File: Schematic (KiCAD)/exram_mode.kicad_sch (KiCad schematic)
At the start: 94 parts

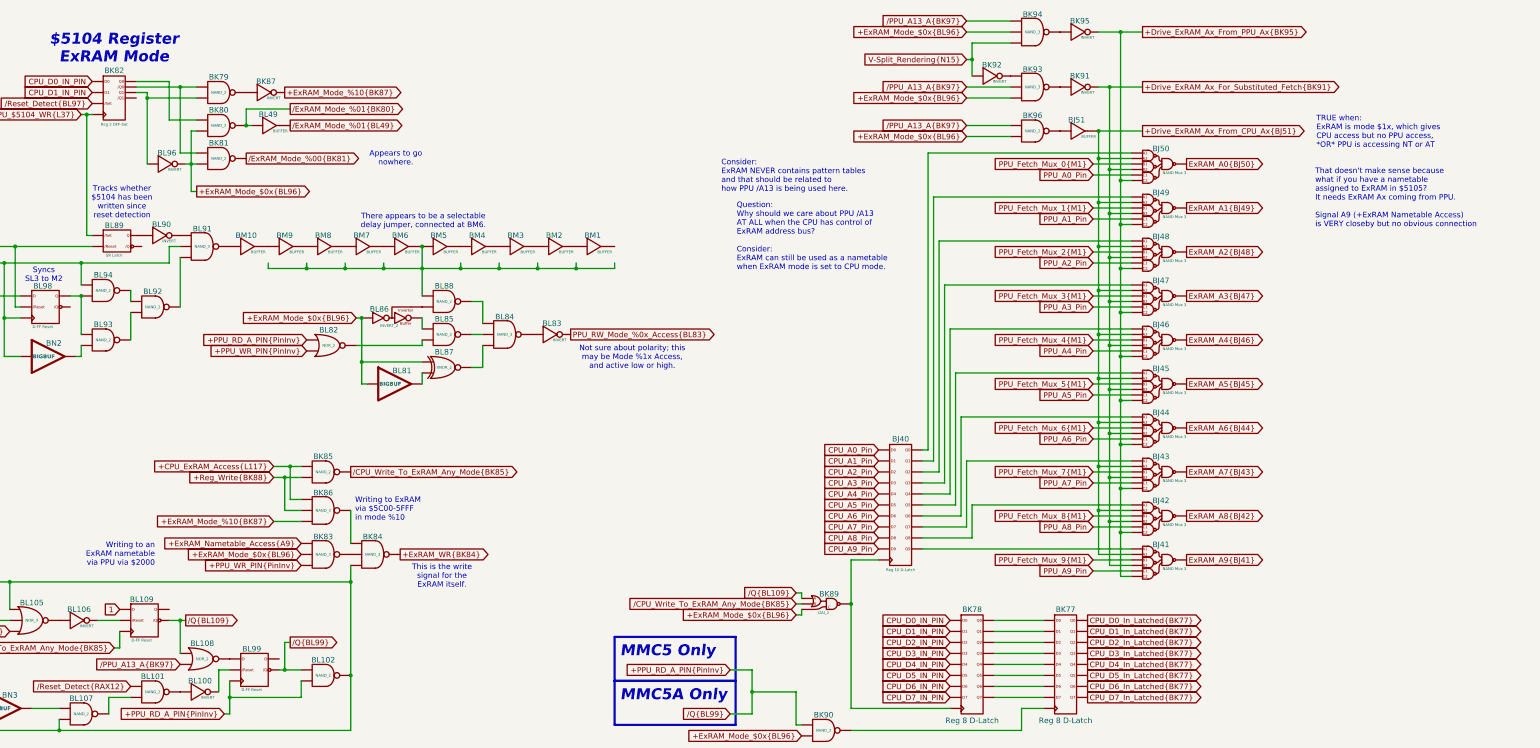
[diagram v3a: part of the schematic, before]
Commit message: Tracing and schematic updates.  - Added timer to schematic.  - Added all items from artifacts sheet to the MMC5A trace.
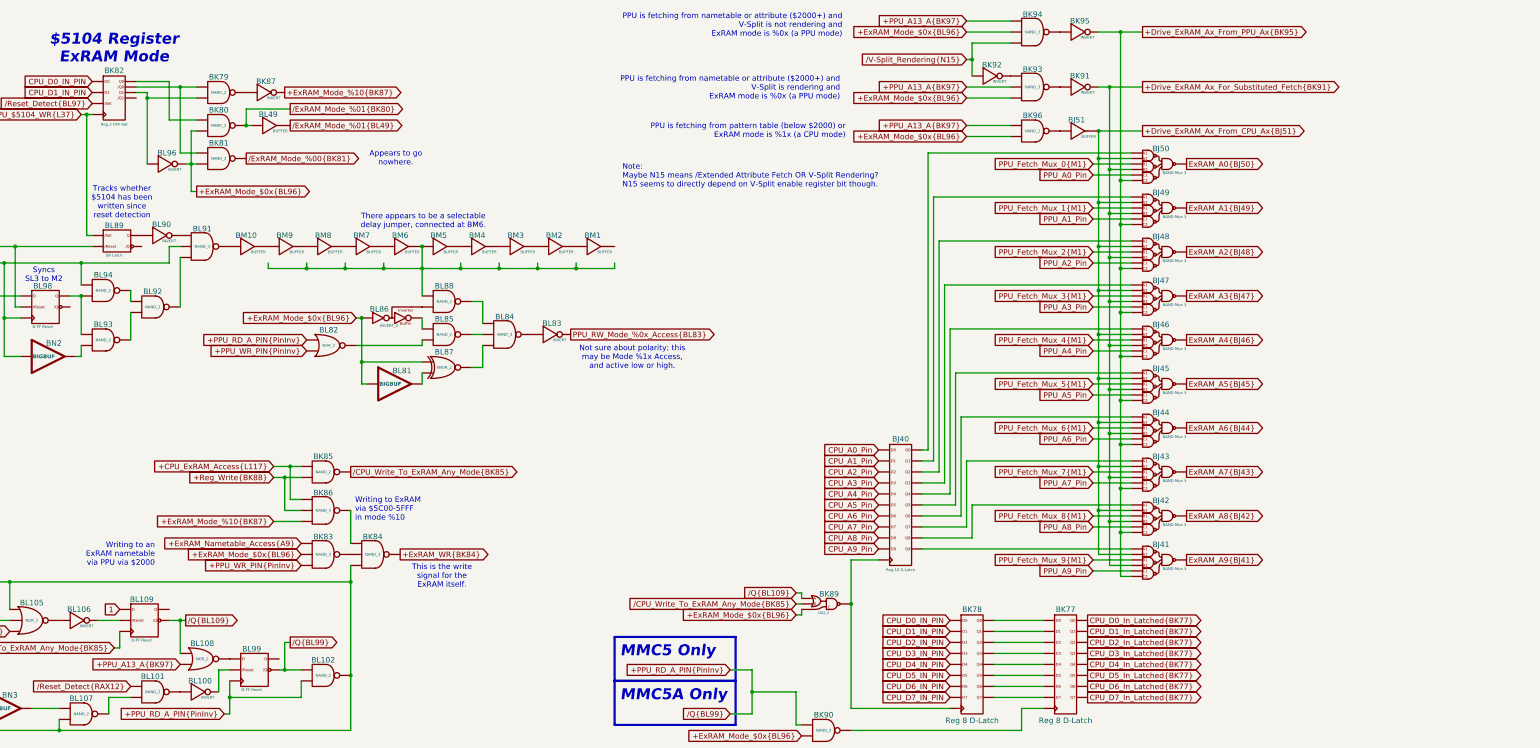
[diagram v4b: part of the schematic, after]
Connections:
- net V-Split_Rendering{N15} is gone; now on net /V-Split_Rendering{N15}: BK92. (X), BK94. (X)
- net at BL100. (X): now also BL101. (X); no longer BL99. (/Q)
- net +PPU_A13_A{BK97}: now reaches BK93. (X)
- net +PPU_A13_A{BK97}: now also BK94. (X), BK96. (X), BL108. (X); no longer BK91. (X)
- net at BL90. (X): now also BL91. (X); no longer BL89. (/Q)
- net /V-Split_Rendering{N15}: now reaches BK92. (X)
- net /V-Split_Rendering{N15}: no longer BK93. (X)
- net at BL93. (X): now also BL92. (X); no longer BN2. (X)
- net at BJ10. (X): now also BJ11. (/Q7); no longer BJ9. (X)
- net at BL88. (X): now also BL86. (X); no longer BL84. (X)
- net at BL92. (X): now also BL94. (X); no longer BL93. (X)
- net at BM9. (X): now also BM10. (X); no longer BM8. (X)
- net at BM10. (X): now also BL91. (X); no longer BM9. (X)
- net at BL84. (X): now also BL85. (X); no longer BL87. (X)
- net at BL103. (X): now also BJ39b. (X); no longer BL95. (X)
- net at BL85. (X): now also BL86. (X); no longer BL82. (X)
- net at BM3. (X): now also BM4. (X); no longer BM2. (X)
- net at BM4. (X): now also BM5. (X); no longer BM3. (X)
- net at BL106. (X): now also BL109. (/Q); no longer BL105. (X)
- removed net /PPU_A13_A{BK97}: BK93. (X), BK94. (X), BK96. (X), BL108. (X)
- new net: BL81. (X), BL87. (X)
- new net: BJ40. (Q9), BK78. (Q7), BK89. (X)
- new net: BK84. (X), BL102. (X), BL105. (X), BL107. (X), BN3. (X), BN4. (X)
- new net: BK83. (X), BK84. (X)
- new net: BK84. (X), BK86. (X)
- new net: BL108. (X), BL99. (/Q)
- new net: BL100. (X), BL99. (/Q)
- new net: BL93. (X), BL94. (X), BL98. (/Q)
- new net: BJ40. (Q9), BJ43. (X)
- new net: BK91. (X), BK93. (X)
- new net: BK77. (Q7), BK90. (X)
- new net: BK77. (Q7), BK78. (Q7) (x8)
- new net: BK79. (X), BK81. (X), BK82. (Q1)
- new net: BL89. (/Q), BL90. (X)
- new net: BK92. (X), BK93. (X)
- new net: BL93. (X), BN2. (X)
- new net: BJ7. (X), BJ9. (X)
- new net: BJ10. (X), BJ9. (X)
- new net: BJ32. (X), BJ33. (X), BJ34. (X), BJ35. (X), BJ36. (X), BJ37. (X), BJ38. (X), BJ39. (X), BJ39b. (X) (x2)
- new net: BL84. (X), BL88. (X)
- new net: BL88. (X), BM5. (X), BM6. (X)
- new net: BM8. (X), BM9. (X)
- new net: BK79. (X), BK82. (Q1), BL96. (X)
- new net: BL84. (X), BL87. (X)
- new net: BL104. (X), BL95. (X)
- new net: BL103. (X), BL95. (X)
- new net: BL82. (X), BL85. (X)
- new net: BL83. (X), BL84. (X)
- new net: BJ51. (X), BK96. (X)
- new net: BM2. (X), BM3. (X)
- new net: BK80. (X), BK82. (Q1)
- new net: BL105. (X), BL106. (X)
- new net: BL91. (X), BL92. (X)
- new net: BJ40. (Q9), BJ50. (X)
- new net: BJ40. (Q9), BJ46. (X)
- new net: BJ40. (Q9), BJ42. (X)
- new net: BJ40. (Q9), BJ44. (X)
- new net: BJ40. (Q9), BJ49. (X)
- new net: BJ40. (Q9), BJ45. (X)
- new net: BJ40. (Q9), BJ48. (X)
- new net: BJ40. (Q9), BJ47. (X)
- new net: BJ40. (Q9), BJ41. (X)
- new net: BK94. (X), BK95. (X)
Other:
- note added: "Note: Maybe N15 means /Extended Attribute Fetch OR V-Split Rendering? N15 seems to directly depend on V-Split enable register bit though."
- note added: "PPU is fetching from nametable or attribute ($2000+) and V-Split is not rendering and ExRAM mode is %0x (a PPU mode)"
- note added: "PPU is fetching from nametable or attribute ($2000+) and V-Split is rendering and ExRAM mode is %0x (a PPU mode)"
- note added: "PPU is fetching from pattern table (below $2000) or ExRAM mode is %1x (a CPU mode)"
- note removed: "Consider: ExRAM NEVER contains pattern tables and that should be related to how PPU /A13 is being used here."
- note removed: "Question: Why should we care about PPU /A13 AT ALL when the CPU has control of ExRAM address bus? Consider: ExRAM can still be used as a nametable when ExRAM mode is set to CPU mode."
- note removed: "TRUE when: ExRAM is mode $1x, which gives CPU access but no PPU access, *OR* PPU is accessing NT or AT"
- note removed: "That doesn't make sense because what if you have a nametable assigned to ExRAM in $5105? It needs ExRAM Ax coming from PPU. Signal A9 (+ExRAM Nametable Access) is VERY closeby but no obvious connection"
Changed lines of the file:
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@@
 		)
 	)
-	(text "Question:\nWhy should we care about PPU /A13\nAT ALL when the CPU has control of\nExRAM address bus?\n\nConsider:\nExRAM can still be used as a nametable\nwhen ExRAM mode is set to CPU mode."
+	(text "PPU is fetching from pattern table (below $2000) or\nExRAM mode is %1x (a CPU mode)"
 		(exclude_from_sim no)
-		(at 217.424 68.834 0)
+		(at 242.57 44.45 0)
 		(effects
 			(font
 				(size 1.27 1.27)
 			)
-			(justify left)
+			(justify right)
 		)
 	)
@@
 		)
 	)
-	(text "That doesn't make sense because\nwhat if you have a nametable\nassigned to ExRAM in $5105?\nIt needs ExRAM Ax coming from PPU.\n\nSignal A9 (+ExRAM Nametable Access)\nis VERY closeby but no obvious connection"
+	(text "PPU is fetching from nametable or attribute ($2000+) and\nV-Split is not rendering and\nExRAM mode is %0x (a PPU mode)"
 		(exclude_from_sim no)
-		(at 351.028 59.944 0)
+		(at 241.808 20.066 0)
 		(effects
 			(font
 				(size 1.27 1.27)
 			)
-			(justify left)
+			(justify right)
 		)
 	)
@@
 		)
 	)
-	(text "TRUE when:\nExRAM is mode $1x, which gives\nCPU access but no PPU access,\n*OR* PPU is accessing NT or AT"
+	(text "PPU is fetching from nametable or attribute ($2000+) and\nV-Split is rendering and\nExRAM mode is %0x (a PPU mode)"
 		(exclude_from_sim no)
-		(at 351.282 44.704 0)
+		(at 241.3 34.544 0)
 		(effects
 			(font
 				(size 1.27 1.27)
 			)
-			(justify left)
+			(justify right)
 		)
 	)
@@
 		)
 	)
-	(text "Consider:\nExRAM NEVER contains pattern tables\nand that should be related to\nhow PPU /A13 is being used here."
-		(exclude_from_sim no)
-		(at 213.868 54.864 0)
-		(effects
-			(font
-				(size 1.27 1.27)
-			)
-			(justify left)
-		)
-	)
 	(text "Tracks whether\n$5104 has been\nwritten since\nreset detection"
 		(exclude_from_sim no)
@@
 		)
 	)
+	(text "Note:\nMaybe N15 means /Extended Attribute Fetch OR V-Split Rendering?\nN15 seems to directly depend on V-Split enable register bit though."
+		(exclude_from_sim no)
+		(at 191.008 54.864 0)
+		(effects
+			(font
+				(size 1.27 1.27)
+			)
+			(justify left)
+		)
+	)
 	(text "Writing to an\nExRAM nametable\nvia PPU via $2000"
 		(exclude_from_sim no)
@@
 		)
 	)
-	(global_label "{slash}PPU_A13_A{BK97}"
+	(global_label "+PPU_A13_A{BK97}"
 		(shape input)
 		(at 270.51 34.29 180)
@@
 		)
 		(property "Intersheetrefs" "${INTERSHEET_REFS}"
-			(at 249.14 34.29 0)
+			(at 248.8981 34.29 0)
 			(effects
 				(font
@@
 		)
 	)
-	(global_label "{slash}PPU_A13_A{BK97}"
+	(global_label "+PPU_A13_A{BK97}"
 		(shape input)
 		(at 270.51 19.05 180)
@@
 		)
 		(property "Intersheetrefs" "${INTERSHEET_REFS}"
-			(at 249.14 19.05 0)
+			(at 248.8981 19.05 0)
 			(effects
 				(font
@@
 		)
 	)
-	(global_label "{slash}PPU_A13_A{BK97}"
+	(global_label "+PPU_A13_A{BK97}"
 		(shape input)
 		(at 88.9 167.64 180)
@@
 		)
 		(property "Intersheetrefs" "${INTERSHEET_REFS}"
-			(at 67.53 167.64 0)
+			(at 67.2881 167.64 0)
 			(effects
 				(font
@@
 		)
 	)
-	(global_label "V-Split_Rendering{N15}"
+	(global_label "{slash}V-Split_Rendering{N15}"
 		(shape input)
 		(at 270.51 27.94 180)
@@
 		)
 		(property "Intersheetrefs" "${INTERSHEET_REFS}"
-			(at 244.6649 27.94 0)
+			(at 243.3344 27.94 0)
 			(effects
 				(font
@@
 		)
 	)
-	(global_label "{slash}PPU_A13_A{BK97}"
+	(global_label "+PPU_A13_A{BK97}"
 		(shape input)
 		(at 270.51 43.18 180)
@@
 		)
 		(property "Intersheetrefs" "${INTERSHEET_REFS}"
-			(at 249.14 43.18 0)
+			(at 248.8981 43.18 0)
 			(effects
 				(font
